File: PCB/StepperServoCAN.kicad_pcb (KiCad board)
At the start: 2 copper layers, 56 x 42.8 mm, 108 parts, among them J1 CAR, J2 Debug, J3 Motor, Q1 AO3401A, Q2 AO3401A, Q3 AO3400A, Q4 AO3400A, Q5 BSS84, SW1 Rst, SW2 Fcn>, U1 XL1509-adj, U10 LMV321, U2 TLE5012B, U3 SN65HVD230, U4 STM32F103CBT6, U5 A4950E, U6 A4950E, U8 LMV321, Y1 16Mhz 9pF

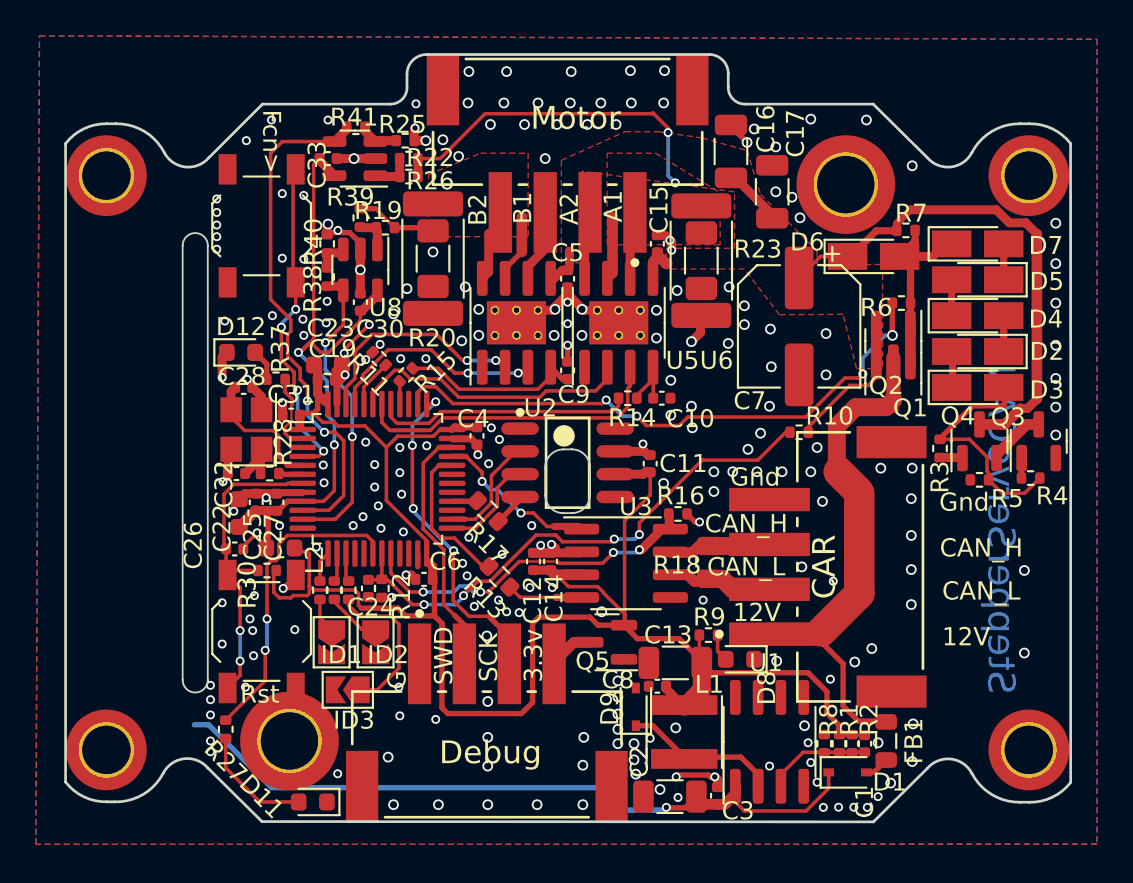
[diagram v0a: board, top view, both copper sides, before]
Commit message: Swapped red/blue LED. Rearranged related tracks.
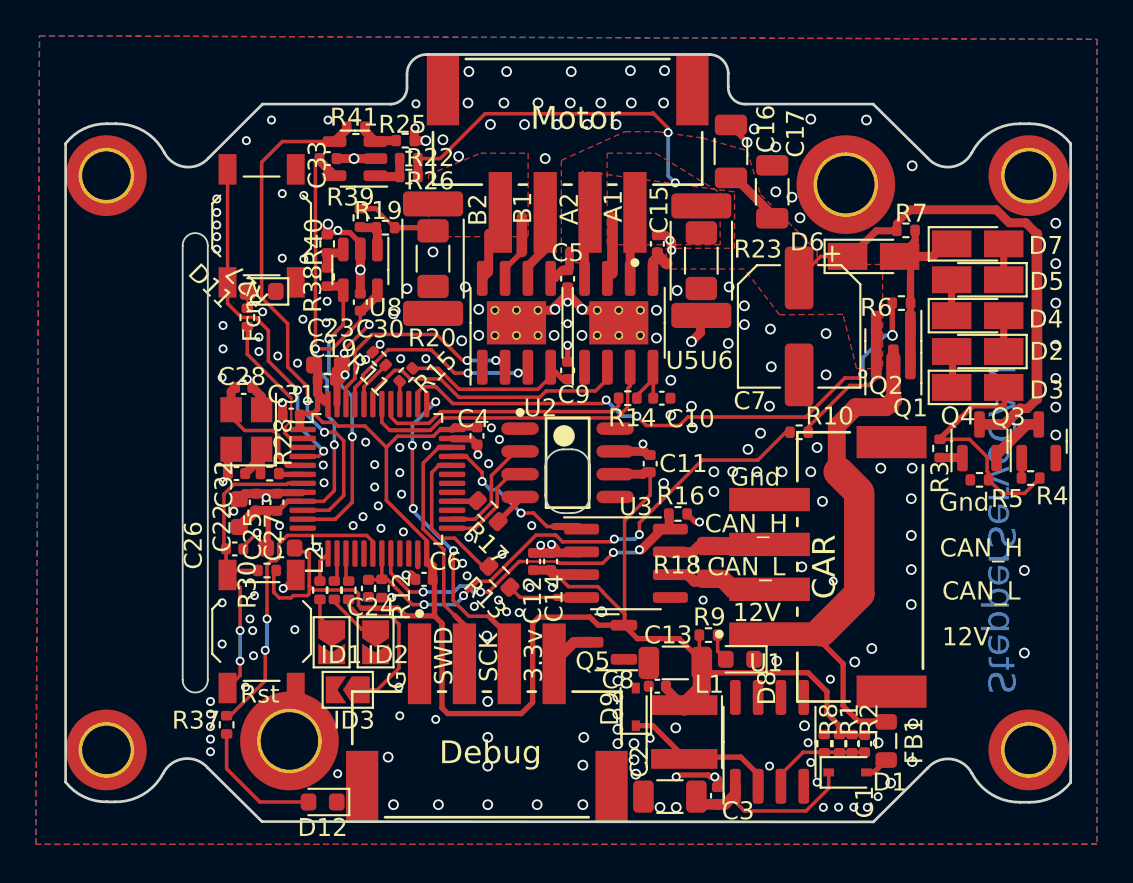
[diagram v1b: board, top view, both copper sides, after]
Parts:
- moved D11 28.6 mm to (83.0, 90.5)
- moved D12 25.5 mm to (86.3, 118.9), turned to 180 degrees
- moved R27 23.0 mm to (82.2, 91.9), turned to 90 degrees
- moved R37 19.4 mm to (81.0, 114.6), turned to 90 degrees
- turned SW2 to 90 degrees
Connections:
- R27 pad 1: Net-(R27-Pad1) -> Net-(U4-Pad2)
- R37 pad 2: Net-(R37-Pad2) -> Net-(U4-Pad18)
- U4 pad 18: Net-(R27-Pad1) -> Net-(U4-Pad18)
- U4 pad 2: Net-(R37-Pad2) -> Net-(U4-Pad2)
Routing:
- net /BATT_Diode: track 41.0 -> 10.7 mm, vias 1 -> 0
- net Net-(R27-Pad1): track 17.4 -> 0.00 mm, vias 2 -> 0
- net Net-(U4-Pad18): track 0.00 -> 17.3 mm, vias 0 -> 2
- net Net-(U4-Pad2): track 0.00 -> 8.16 mm
- net Net-(D11-Pad2): track 6.49 -> 0.95 mm
- net Net-(D12-Pad2): track 1.77 -> 7.27 mm
- net Net-(R37-Pad2): track 4.39 -> 0.00 mm
- net +3.3VA: track 36.1 -> 33.9 mm
- net GND: track 50.5 -> 48.9 mm, vias 230 -> 234
- net /Switch: track 18.4 -> 19.7 mm, vias 4 -> 2

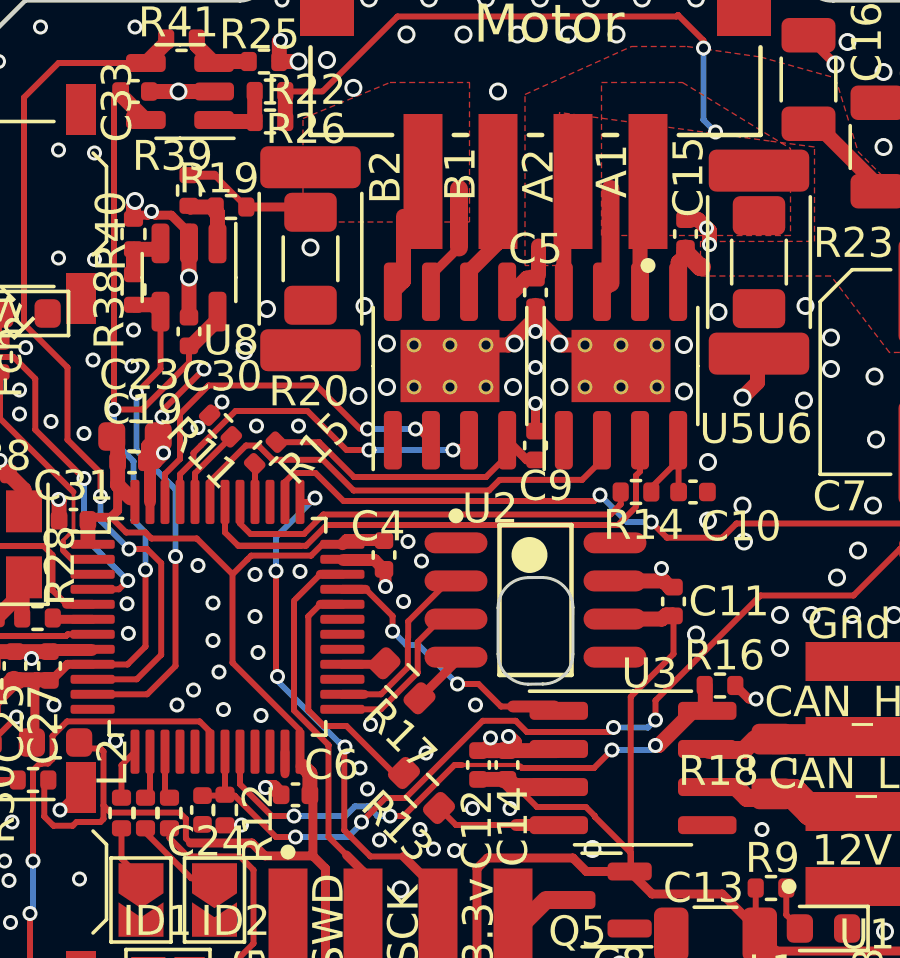
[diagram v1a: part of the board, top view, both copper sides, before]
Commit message: Filled copper around A4950 for better thermals
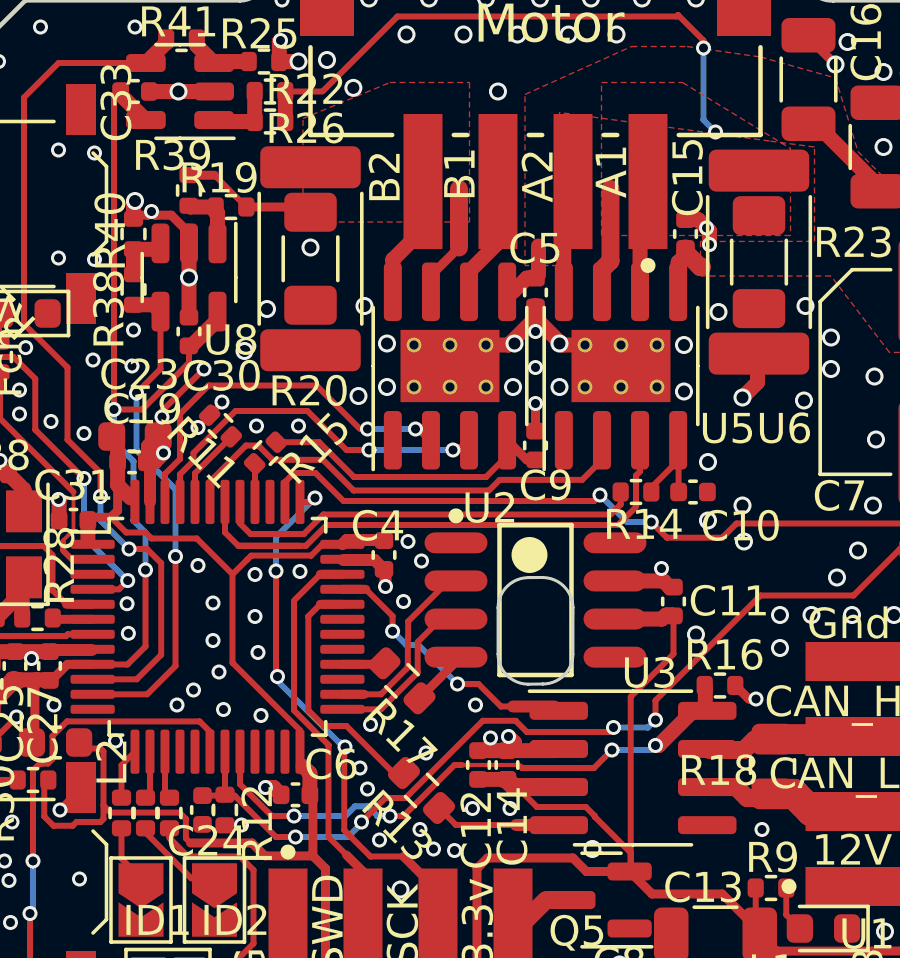
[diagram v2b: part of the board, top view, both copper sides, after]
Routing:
- net GND: track 48.9 -> 48.2 mm
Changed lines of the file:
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@@
   (segment (start 97.785 89.05495) (end 98.75 88.08995) (width 0.5) (layer "F.Cu") (net 7))
   (segment (start 98.75 88.08995) (end 98.75 86.05) (width 0.5) (layer "F.Cu") (net 7))
-  (segment (start 95.245 89.725) (end 95.6 89.37) (width 0.5) (layer "F.Cu") (net 8))
-  (segment (start 95.6 89.37) (end 95.6 87.21) (width 0.5) (layer "F.Cu") (net 8))
+  (segment (start 95.245 89.725) (end 95.245 88.655) (width 0.5) (layer "F.Cu") (net 8))
+  (segment (start 95.245 88.655) (end 96.145 87.755) (width 0.5) (layer "F.Cu") (net 8))
   (segment (start 85.2145 101.66675) (end 83.90325 101.66675) (width 0.4) (layer "F.Cu") (net 10))
   (segment (start 83.90325 101.653) (end 83.83625 101.72) (width 0.4) (layer "F.Cu") (net 10))
@@
   (segment (start 104.6 99.57) (end 104.47 99.57) (width 0.5) (layer "F.Cu") (net 10))
   (segment (start 98.5 104.62) (end 98.1 105.02) (width 0.2) (layer "F.Cu") (net 10))
-  (segment (start 91.65 105.791553) (end 91.65 105.05625) (width 0.3) (layer "F.Cu") (net 10))
   (segment (start 82.005 101.72) (end 81.7 102.025) (width 0.5) (layer "F.Cu") (net 10))
   (segment (start 86.6 86.75) (end 86.65 86.7) (width 0.5) (layer "F.Cu") (net 10))
@@
   (segment (start 90.65 96.73125) (end 90.65 95.471248) (width 0.2) (layer "F.Cu") (net 17))
   (segment (start 92.85 83.05) (end 91.66 83.05) (width 0.2) (layer "F.Cu") (net 18))
-  (segment (start 102.215 89.725) (end 102.5 89.44) (width 0.5) (layer "F.Cu") (net 18))
   (segment (start 91.66 84.05) (end 91.66 83.05) (width 0.5) (layer "F.Cu") (net 18))
   (segment (start 105.6 81.6) (end 105.6 81.35) (width 0.2) (layer "F.Cu") (net 18))
-  (segment (start 102.5 89.44) (end 102.5 86.3) (width 0.6) (layer "F.Cu") (net 18))
   (segment (start 105.6 81.35) (end 104.75 80.5) (width 0.2) (layer "F.Cu") (net 18))
+  (segment (start 102.25 88.95) (end 102.5 88.7) (width 0.6) (layer "F.Cu") (net 18))
   (segment (start 95.4 80.55) (end 92.9 83.05) (width 0.2) (layer "F.Cu") (net 18))
   (segment (start 104.7 80.55) (end 95.4 80.55) (width 0.2) (layer "F.Cu") (net 18))
+  (segment (start 102.215 89.725) (end 102.215 88.985) (width 0.5) (layer "F.Cu") (net 18))
+  (segment (start 102.5 88.7) (end 102.5 86.3) (width 0.6) (layer "F.Cu") (net 18))
   (segment (start 104.75 80.5) (end 104.7 80.55) (width 0.2) (layer "F.Cu") (net 18))
   (via (at 105.6 81.6) (size 0.5) (drill 0.3) (layers "F.Cu" "B.Cu") (net 18))
@@
   (segment (start 83.15 110.45) (end 83.25 110.35) (width 0.2) (layer "B.Cu") (net 74))
   (segment (start 83.25 110.35) (end 83.25 108.7) (width 0.2) (layer "B.Cu") (net 74))
-  (zone (net 0) (net_name "") (layer "F.Cu") (name "A4950_remove_antenas") (hatch edge 0.508)
-    (connect_pads (clearance 0))
-    (min_thickness 0.254)
-    (keepout (tracks allowed) (vias allowed) (pads allowed) (copperpour not_allowed) (footprints allowed))
-    (fill (thermal_gap 0.3) (thermal_bridge_width 0.508))
-    (polygon
-      (pts
-        (xy 104.75 95.7)
-        (xy 95.2 95.7)
-        (xy 95.2 93.85)
-        (xy 104.75 93.85)
-      )
-    )
-  )
   (zone (net 47) (net_name "VMOT") (layer "F.Cu") (name "Vmot") (hatch edge 0.508)
     (priority 3)
@@
       )
     )
-  )
-  (zone (net 0) (net_name "") (layer "F.Cu") (name "A4950_remove_antenas") (hatch edge 0.508)
-    (connect_pads (clearance 0))
-    (min_thickness 0.254)
-    (keepout (tracks allowed) (vias allowed) (pads allowed) (copperpour not_allowed) (footprints allowed))
-    (fill (thermal_gap 0.3) (thermal_bridge_width 0.508))
-    (polygon
-      (pts
-        (xy 104.85 90.7)
-        (xy 95.3 90.7)
-        (xy 95.3 88.45)
-        (xy 104.85 88.45)
-      )
-    )

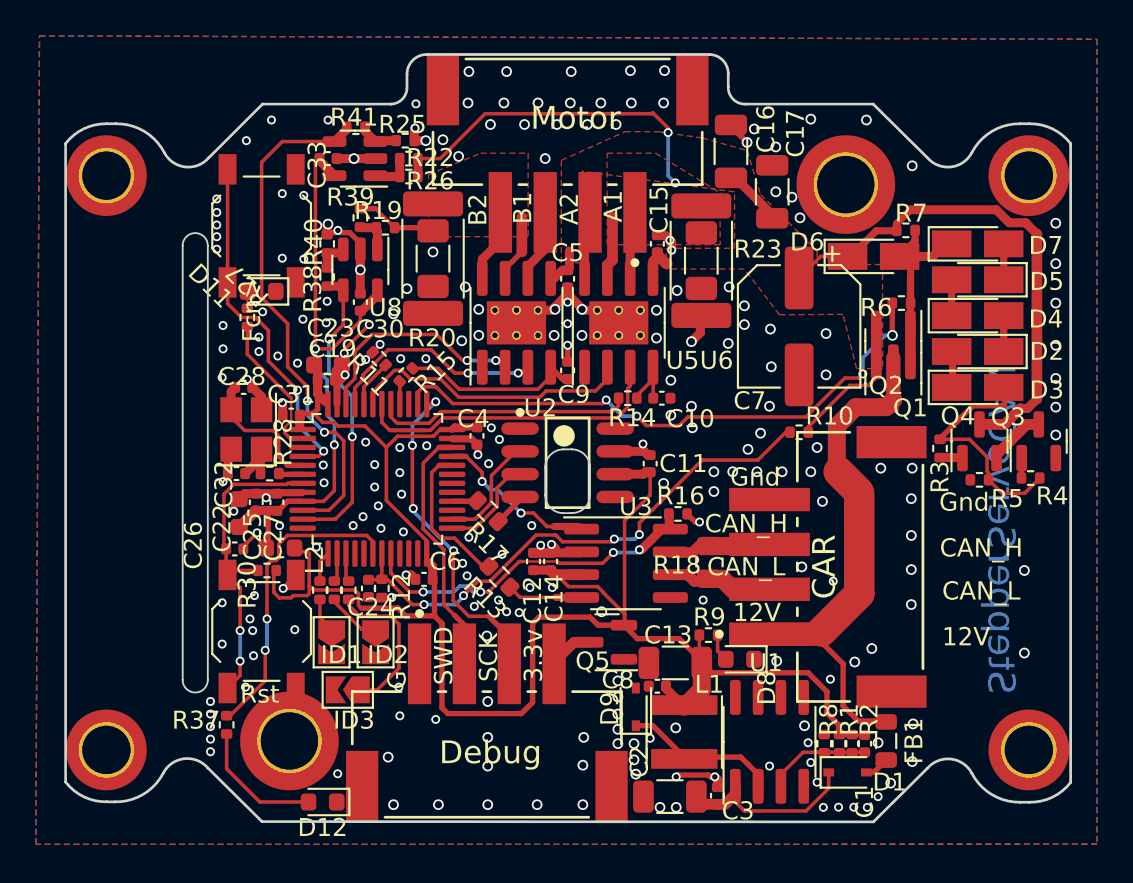
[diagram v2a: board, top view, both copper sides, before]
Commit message: Moved JST connector reference point so that actual connector sticks out more after manufacturing
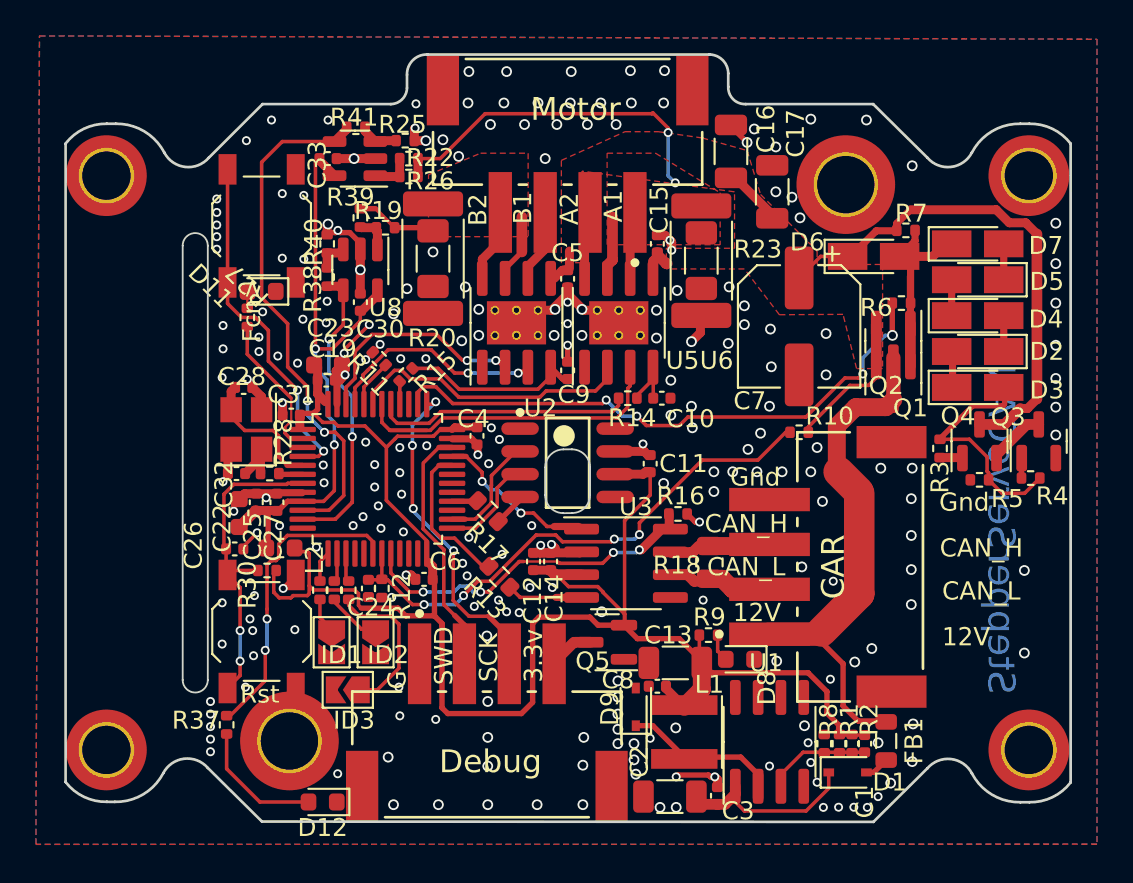
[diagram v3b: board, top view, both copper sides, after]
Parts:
- moved J1 0.50 mm to (114.8, 105.8)
- moved J2 0.50 mm to (95.5, 114.8)
- moved J3 0.50 mm to (100.0, 82.5)

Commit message: Text
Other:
- board text added: "Apply thermal paste ->"
- board text added: "V_Bat max: 30V Phase peak current 3.3A Total RMS current 4.5A"
- board text removed: "V_Bat max: 30V Phase max current 3.3A"
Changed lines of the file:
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@@
   (gr_line (start 100 96.869505) (end 100 103.2) (layer "B.SilkS") (width 0.15))
   (gr_rect (start 119.7 111.55) (end 110.75 99.85) (layer "B.SilkS") (width 0.15) (fill none))
+  (gr_rect (start 93.45 89.65) (end 106.3 94.75) (layer "B.SilkS") (width 0.15) (fill none))
   (gr_rect (start 90.5 103.55) (end 110.15 111.6) (layer "B.SilkS") (width 0.15) (fill none))
   (gr_line (start 103.130495 100) (end 97 100) (layer "B.SilkS") (width 0.15))
@@
     (effects (font (size 1 1) (thickness 0.15)) (justify mirror))
   )
-  (gr_text "V_Bat max: 30V\nPhase max current 3.3A" (at 109.05 108.75) (layer "B.SilkS")
+  (gr_text "V_Bat max: 30V\nPhase peak current 3.3A\nTotal RMS current 4.5A" (at 109.45 108.7) (layer "B.SilkS")
     (effects (font (size 1.016 1) (thickness 0.15)) (justify left mirror))
   )
@@
     (effects (font (size 1 1) (thickness 0.15)) (justify mirror))
   )
+  (gr_text "Apply thermal\npaste ->" (at 106.7 91.45) (layer "B.SilkS")
+    (effects (font (size 1.016 1) (thickness 0.15)) (justify right mirror))
+  )
   (gr_text "Debug" (at 95.25 114.05) (layer "B.SilkS")
